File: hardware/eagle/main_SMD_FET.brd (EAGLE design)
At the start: 40 x 31.8 mm, 43 parts, among them IC1 R-78E3.3-1.0, IC3 ESP-12E/F, IC4 INA301A1IDGKR, J4 1727078, Q1 IPD031N06, Q2 IPD031N06, Q3 IPD031N06, Q4 IPD031N06

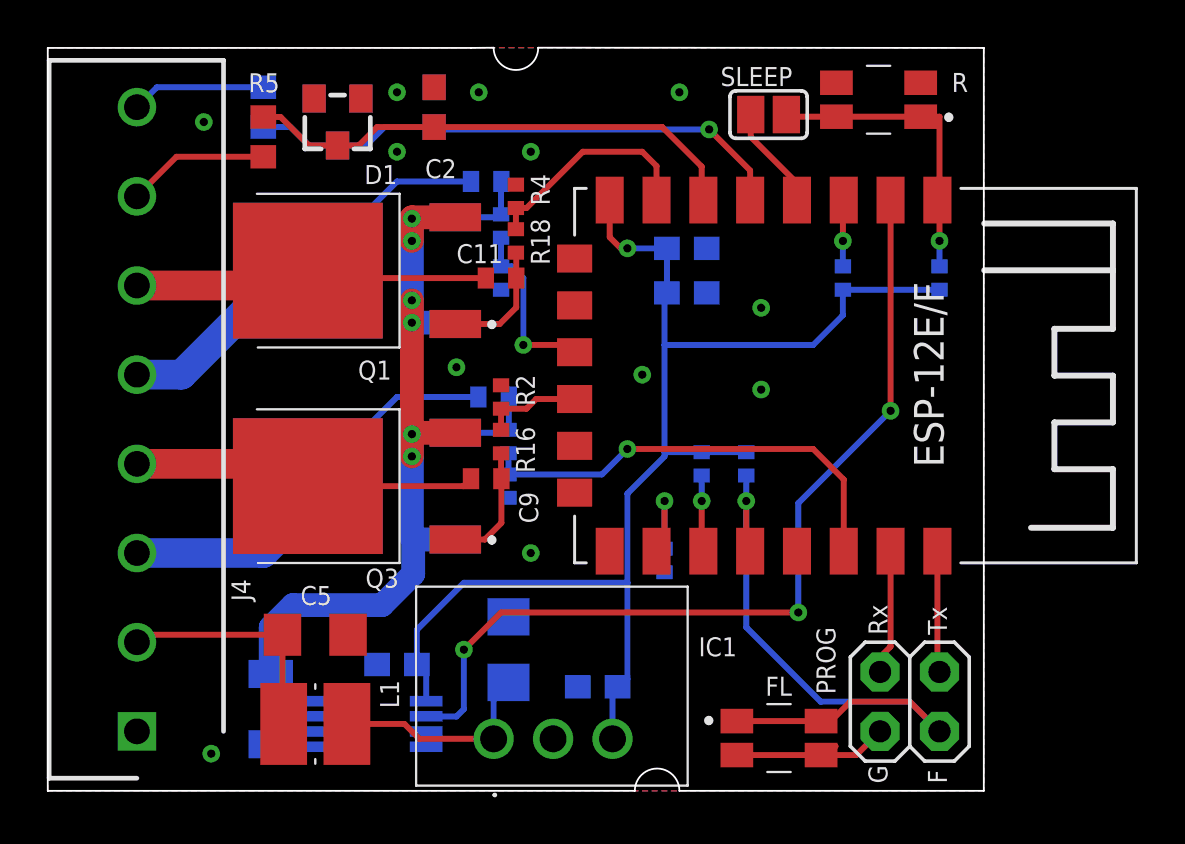
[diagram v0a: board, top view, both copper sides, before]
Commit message: tiefpass eingefügt. Leiterbahn etwas breiter für DC/DC wandler
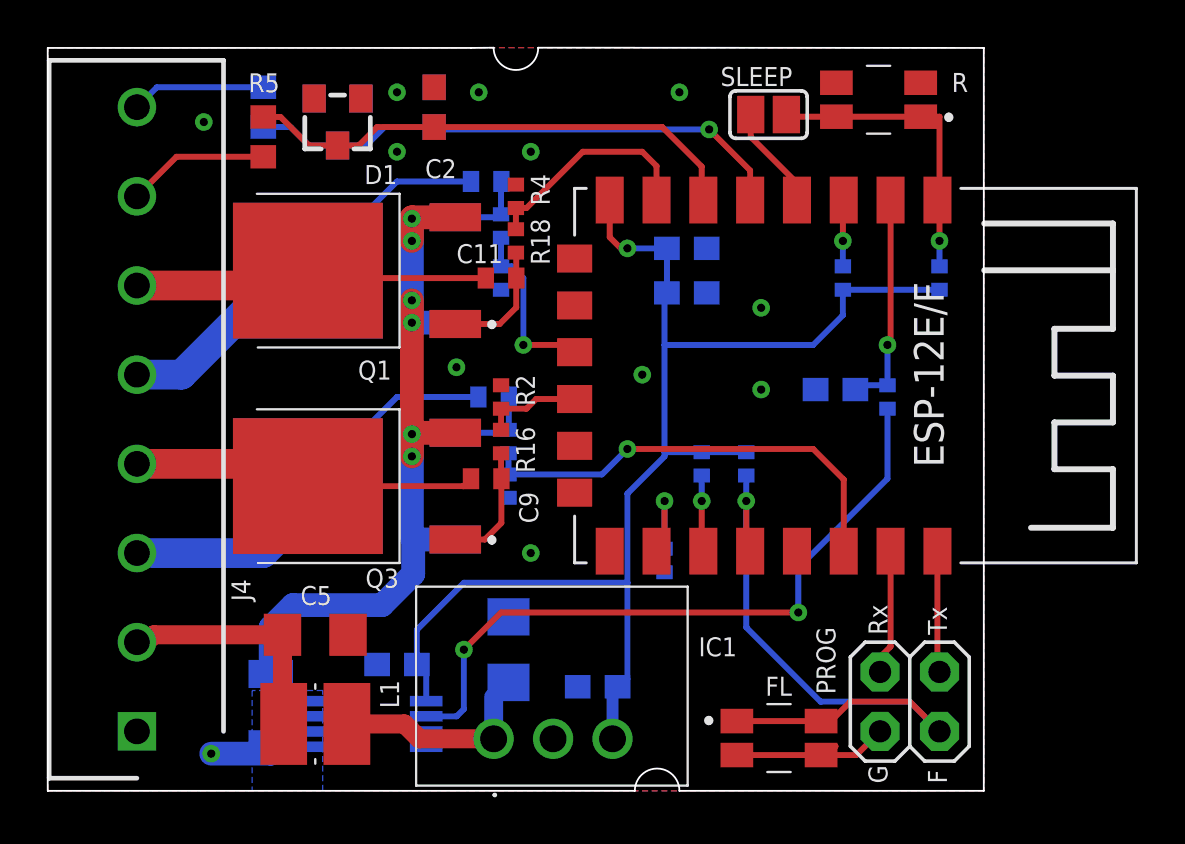
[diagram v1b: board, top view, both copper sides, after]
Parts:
- added C13: 100n, rcl:C0603
- added R13: 10k, rcl:R0402
- C3, C4: value (none) -> 4µ7
- C5: value (none) -> 1µ
- R12: value PCS1206DR0100ET -> 0R005
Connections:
- removed net N$1: IC3.ADC, IC4.2
- new net N$: C13.2, IC3.ADC, R13.2
- new net N$8: IC4.2, R13.1
- net GND: now also C13.1
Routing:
- net N$1: track 38.5 -> 0.00 mm, vias 3 -> 0
- net N$8: track 0.00 -> 29.5 mm, vias 0 -> 2
- net N$: track 0.00 -> 9.42 mm, vias 0 -> 1
- net GND: track 11.3 -> 14.3 mm

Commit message: dokumentation
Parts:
- D1, D2: value BZX84CSMD -> BZX84C3V3
